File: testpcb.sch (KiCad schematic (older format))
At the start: 14 parts

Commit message: pady poustawiane
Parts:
- added D1, D10, D11, D12, D13, D14, D15, D16, D17, D2, D3, D4, D5, D6, D7, D8, D9: D_Small, Diode_SMD:D_SOD-123, symbol Device:D_Small
- added F1: 500mA, Fuse:Fuse_1206_3216Metric, symbol Device:Polyfuse_Small
- added MX1, MX10, MX11, MX12, MX13, MX14, MX15, MX2, MX3, MX4, MX6, MX7, MX8, MX9: MX-NoLED, MX_Only:MXOnly-1U, symbol MX_Alps_Hybrid:MX-NoLED
- added MX16, MX17, MX5: MX-NoLED, MX_Only:MXOnly-2U, symbol MX_Alps_Hybrid:MX-NoLED
- added R5, R6: 5k1, Resistor_SMD:R_0815_2038Metric, symbol Device:R_Small
- added USB1: HRO-TYPE-C-31-M-12, Type-C:HRO-TYPE-C-31-M-12-Assembly, symbol Type-C:HRO-TYPE-C-31-M-12
- C1, C2, C3, C4, C5, C6: renamed from C?; footprint (none) -> Capacitor_SMD:C_0805_2012Metric
- C7: renamed from C?; value C_Small -> 1uF; footprint (none) -> Capacitor_SMD:C_0805_2012Metric
- R1, R2, R3, R4: renamed from R?; footprint (none) -> Resistor_SMD:R_0815_2038Metric
- SW1: renamed from SW?; footprint (none) -> random-keyboard-parts:SKQG-1155865
- Y1: renamed from Y?; footprint (none) -> Crystal:Crystal_SMD_3225-4Pin_3.2x2.5mm
- gave numbers to parts that had none: 1
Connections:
- net +5V: now also F1.1
- net D+: now also USB1.6 (DP1), USB1.8 (DP2)
- net D-: now also USB1.5 (DN2), USB1.7 (DN1)
- net GND: now also R5.1, R6.1, USB1.1 (GND)
- new net: R6.2, USB1.10 (CC2)
- new net: R5.2, USB1.4 (CC1)
- new net: D1.2 (A), MX1.2 (ROW)
- new net: D6.2 (A), MX6.2 (ROW)
- new net: D10.2 (A), MX10.2 (ROW)
- new net: D15.2 (A), MX15.2 (ROW)
- new net: D2.2 (A), MX2.2 (ROW)
- new net: D7.2 (A), MX7.2 (ROW)
- new net: D11.2 (A), MX11.2 (ROW)
- new net: D3.2 (A), MX3.2 (ROW)
- new net: D8.2 (A), MX8.2 (ROW)
- new net: D12.2 (A), MX12.2 (ROW)
- new net: D16.2 (A), MX16.2 (ROW)
- new net: D4.2 (A), MX4.2 (ROW)
- new net: D9.2 (A), MX9.2 (ROW)
- new net: D13.2 (A), MX13.2 (ROW)
- new net: D5.2 (A), MX5.2 (ROW)
- new net: D14.2 (A), MX14.2 (ROW)
- new net: D17.2 (A), MX17.2 (ROW)
- new net COL0: MX1.1 (COL), MX2.1 (COL), MX3.1 (COL), MX4.1 (COL), MX5.1 (COL)
- new net COL1: MX6.1 (COL), MX7.1 (COL), MX8.1 (COL), MX9.1 (COL)
- new net COL2: MX10.1 (COL), MX11.1 (COL), MX12.1 (COL), MX13.1 (COL), MX14.1 (COL)
- new net COL3: MX15.1 (COL), MX16.1 (COL), MX17.1 (COL)
- new net ROW0: D1.1 (K), D10.1 (K), D15.1 (K), D6.1 (K)
- new net ROW1: D11.1 (K), D16.1 (K), D2.1 (K), D7.1 (K)
- new net ROW2: D12.1 (K), D3.1 (K), D8.1 (K)
- new net ROW3: D13.1 (K), D17.1 (K), D4.1 (K), D9.1 (K)
- new net ROW4: D14.1 (K), D5.1 (K)
- new net VCC: F1.2, USB1.2 (VBUS)
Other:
- moved on the sheet: C1, C2, C5, C6

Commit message: ulozenie git
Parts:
- R1, R2, R3, R4, R5, R6: footprint Resistor_SMD:R_0815_2038Metric -> Resistor_SMD:R_0805_2012Metric
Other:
- moved on the sheet: C1, C2, C5, C6
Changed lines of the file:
@@
 F 0 "R4" V 4154 5750 50  0000 C CNN
 F 1 "10k" V 4245 5750 50  0000 C CNN
-F 2 "Resistor_SMD:R_0815_2038Metric" H 4350 5750 50  0001 C CNN
+F 2 "Resistor_SMD:R_0805_2012Metric" H 4350 5750 50  0001 C CNN
 F 3 "~" H 4350 5750 50  0001 C CNN
 	1    4350 5750
@@
 F 0 "R2" V 1704 4650 50  0000 C CNN
 F 1 "22" V 1795 4650 50  0000 C CNN
-F 2 "Resistor_SMD:R_0815_2038Metric" H 1900 4650 50  0001 C CNN
+F 2 "Resistor_SMD:R_0805_2012Metric" H 1900 4650 50  0001 C CNN
 F 3 "~" H 1900 4650 50  0001 C CNN
 	1    1900 4650
@@
 F 0 "R1" V 1354 4750 50  0000 C CNN
 F 1 "22" V 1445 4750 50  0000 C CNN
-F 2 "Resistor_SMD:R_0815_2038Metric" H 1550 4750 50  0001 C CNN
+F 2 "Resistor_SMD:R_0805_2012Metric" H 1550 4750 50  0001 C CNN
 F 3 "~" H 1550 4750 50  0001 C CNN
 	1    1550 4750
@@
 L power:+5V #PWR0105
 U 1 1 60AE12C3
-P 1700 1300
-F 0 "#PWR0105" H 1700 1150 50  0001 C CNN
-F 1 "+5V" H 1715 1473 50  0000 C CNN
-F 2 "" H 1700 1300 50  0001 C CNN
-F 3 "" H 1700 1300 50  0001 C CNN
-	1    1700 1300
+P 1950 1350
+F 0 "#PWR0105" H 1950 1200 50  0001 C CNN
+F 1 "+5V" H 1965 1523 50  0000 C CNN
+F 2 "" H 1950 1350 50  0001 C CNN
+F 3 "" H 1950 1350 50  0001 C CNN
+	1    1950 1350
 	1    0    0    -1
 $EndComp
@@
 L Device:C_Small C1
 U 1 1 60AE244A
-P 1100 1500
-F 0 "C1" H 1192 1546 50  0000 L CNN
-F 1 "0.1uF" H 1192 1455 50  0000 L CNN
-F 2 "Capacitor_SMD:C_0805_2012Metric" H 1100 1500 50  0001 C CNN
-F 3 "~" H 1100 1500 50  0001 C CNN
-	1    1100 1500
+P 1350 1550
+F 0 "C1" H 1442 1596 50  0000 L CNN
+F 1 "0.1uF" H 1442 1505 50  0000 L CNN
+F 2 "Capacitor_SMD:C_0805_2012Metric" H 1350 1550 50  0001 C CNN
+F 3 "~" H 1350 1550 50  0001 C CNN
+	1    1350 1550
 	1    0    0    -1
 $EndComp
@@
 L power:GND #PWR0106
 U 1 1 60AE1A76
-P 1700 1700
-F 0 "#PWR0106" H 1700 1450 50  0001 C CNN
-F 1 "GND" H 1705 1527 50  0000 C CNN
-F 2 "" H 1700 1700 50  0001 C CNN
-F 3 "" H 1700 1700 50  0001 C CNN
-	1    1700 1700
+P 1950 1750
+F 0 "#PWR0106" H 1950 1500 50  0001 C CNN
+F 1 "GND" H 1955 1577 50  0000 C CNN
+F 2 "" H 1950 1750 50  0001 C CNN
+F 3 "" H 1950 1750 50  0001 C CNN
+	1    1950 1750
 	1    0    0    -1
 $EndComp
@@
 L Device:C_Small C2
 U 1 1 60AE4BA8
-P 1500 1500
-F 0 "C2" H 1592 1546 50  0000 L CNN
-F 1 "0.1uF" H 1592 1455 50  0000 L CNN
-F 2 "Capacitor_SMD:C_0805_2012Metric" H 1500 1500 50  0001 C CNN
-F 3 "~" H 1500 1500 50  0001 C CNN
-	1    1500 1500
+P 1750 1550
+F 0 "C2" H 1842 1596 50  0000 L CNN
+F 1 "0.1uF" H 1842 1505 50  0000 L CNN
+F 2 "Capacitor_SMD:C_0805_2012Metric" H 1750 1550 50  0001 C CNN
+F 3 "~" H 1750 1550 50  0001 C CNN
+	1    1750 1550
 	1    0    0    -1
 $EndComp
@@
 L Device:C_Small C5
 U 1 1 60AE54EF
-P 1900 1500
-F 0 "C5" H 1992 1546 50  0000 L CNN
-F 1 "0.1uF" H 1992 1455 50  0000 L CNN
-F 2 "Capacitor_SMD:C_0805_2012Metric" H 1900 1500 50  0001 C CNN
-F 3 "~" H 1900 1500 50  0001 C CNN
-	1    1900 1500
+P 2150 1550
+F 0 "C5" H 2242 1596 50  0000 L CNN
+F 1 "0.1uF" H 2242 1505 50  0000 L CNN
+F 2 "Capacitor_SMD:C_0805_2012Metric" H 2150 1550 50  0001 C CNN
+F 3 "~" H 2150 1550 50  0001 C CNN
+	1    2150 1550
 	1    0    0    -1
 $EndComp
@@
 L Device:C_Small C6
 U 1 1 60AE5F61
-P 2300 1500
-F 0 "C6" H 2392 1546 50  0000 L CNN
-F 1 "10uF" H 2392 1455 50  0000 L CNN
-F 2 "Capacitor_SMD:C_0805_2012Metric" H 2300 1500 50  0001 C CNN
-F 3 "~" H 2300 1500 50  0001 C CNN
-	1    2300 1500
-	1    0    0    -1
-$EndComp
-Wire Wire Line
-	1100 1400 1500 1400
-Connection ~ 1500 1400
-Wire Wire Line
-	1500 1400 1700 1400
-Connection ~ 1900 1400
-Wire Wire Line
-	1900 1400 2300 1400
-Wire Wire Line
-	2300 1600 1900 1600
-Connection ~ 1500 1600
-Wire Wire Line
-	1500 1600 1100 1600
-Connection ~ 1900 1600
-Wire Wire Line
-	1900 1600 1700 1600
-Wire Wire Line
-	1700 1700 1700 1600
-Connection ~ 1700 1600
-Wire Wire Line
-	1700 1600 1500 1600
-Wire Wire Line
-	1700 1300 1700 1400
-Connection ~ 1700 1400
-Wire Wire Line
-	1700 1400 1900 1400
+P 2550 1550
+F 0 "C6" H 2642 1596 50  0000 L CNN
+F 1 "10uF" H 2642 1505 50  0000 L CNN
+F 2 "Capacitor_SMD:C_0805_2012Metric" H 2550 1550 50  0001 C CNN
+F 3 "~" H 2550 1550 50  0001 C CNN
+	1    2550 1550
+	1    0    0    -1
+$EndComp
+Wire Wire Line
+	1350 1450 1750 1450
+Connection ~ 1750 1450
+Wire Wire Line
+	1750 1450 1950 1450
+Connection ~ 2150 1450
+Wire Wire Line
+	2150 1450 2550 1450
+Wire Wire Line
+	2550 1650 2150 1650
+Connection ~ 1750 1650
+Wire Wire Line
+	1750 1650 1350 1650
+Connection ~ 2150 1650
+Wire Wire Line
+	2150 1650 1950 1650
+Wire Wire Line
+	1950 1750 1950 1650
+Connection ~ 1950 1650
+Wire Wire Line
+	1950 1650 1750 1650
+Wire Wire Line
+	1950 1350 1950 1450
+Connection ~ 1950 1450
+Wire Wire Line
+	1950 1450 2150 1450
 $Comp
 L power:+5V #PWR0107
@@
 F 0 "R3" H 2759 3196 50  0000 L CNN
 F 1 "10k" H 2759 3105 50  0000 L CNN
-F 2 "Resistor_SMD:R_0815_2038Metric" H 2700 3150 50  0001 C CNN
+F 2 "Resistor_SMD:R_0805_2012Metric" H 2700 3150 50  0001 C CNN
 F 3 "~" H 2700 3150 50  0001 C CNN
 	1    2700 3150
@@
 F 0 "R5" V 6354 3000 50  0000 C CNN
 F 1 "5k1" V 6445 3000 50  0000 C CNN
-F 2 "Resistor_SMD:R_0815_2038Metric" H 6550 3000 50  0001 C CNN
+F 2 "Resistor_SMD:R_0805_2012Metric" H 6550 3000 50  0001 C CNN
 F 3 "~" H 6550 3000 50  0001 C CNN
 	1    6550 3000
@@
 F 0 "R6" V 6354 3300 50  0000 C CNN
 F 1 "5k1" V 6445 3300 50  0000 C CNN
-F 2 "Resistor_SMD:R_0815_2038Metric" H 6550 3300 50  0001 C CNN
+F 2 "Resistor_SMD:R_0805_2012Metric" H 6550 3300 50  0001 C CNN
 F 3 "~" H 6550 3300 50  0001 C CNN
 	1    6550 3300

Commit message: jakies poprawki chyba
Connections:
- net GND: now also USB1.12 (GND), USB1.13 (SHIELD)
- net VCC: now also USB1.11 (VBUS)
- no-connect marks 0 -> 2
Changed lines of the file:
@@
 Text GLabel 6250 2900 2    50   Input ~ 0
 D+
+NoConn ~ 5850 2600
+NoConn ~ 5850 3200
+$Comp
+L power:GND #PWR0115
+U 1 1 60B55626
+P 6100 3500
+F 0 "#PWR0115" H 6100 3250 50  0001 C CNN
+F 1 "GND" H 6105 3327 50  0000 C CNN
+F 2 "" H 6100 3500 50  0001 C CNN
+F 3 "" H 6100 3500 50  0001 C CNN
+	1    6100 3500
+	1    0    0    -1
+$EndComp
+Wire Wire Line
+	5850 3500 6100 3500
+Wire Wire Line
+	5850 3600 5850 3500
+Connection ~ 5850 3500
+$Comp
+L power:VCC #PWR0116
+U 1 1 60B6523D
+P 6300 3450
+F 0 "#PWR0116" H 6300 3300 50  0001 C CNN
+F 1 "VCC" H 6315 3623 50  0000 C CNN
+F 2 "" H 6300 3450 50  0001 C CNN
+F 3 "" H 6300 3450 50  0001 C CNN
+	1    6300 3450
+	1    0    0    -1
+$EndComp
+Wire Wire Line
+	5850 3400 6250 3400
+Wire Wire Line
+	6250 3400 6250 3450
+Wire Wire Line
+	6250 3450 6300 3450
 $EndSCHEMATC

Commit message: polaczone switche / wizualne poprawki tracerow
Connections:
- net COL0: now also U1.28 (PB4)
- net COL1: now also U1.27 (PD7)
- net COL2: now also U1.26 (PD6)
- net COL3: now also U1.25 (PD4)
- net ROW0: now also U1.36 (PF7)
- net ROW1: now also U1.37 (PF6)
- net ROW2: now also U1.38 (PF5)
- net ROW3: now also U1.39 (PF4)
- net ROW4: now also U1.40 (PF1)
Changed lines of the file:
@@
 Wire Wire Line
 	6250 3450 6300 3450
+Wire Wire Line
+	3900 5550 4100 5550
+Wire Wire Line
+	3900 5450 4100 5450
+Wire Wire Line
+	3900 5250 4100 5250
+Wire Wire Line
+	3900 4050 4150 4050
+Text GLabel 4100 5250 2    50   Input ~ 0
+COL3
+Text GLabel 4100 5450 2    50   Input ~ 0
+COL2
+Text GLabel 4100 5550 2    50   Input ~ 0
+COL1
+Text GLabel 4150 4050 2    50   Input ~ 0
+COL0
+Wire Wire Line
+	3900 6550 4200 6550
+Wire Wire Line
+	3900 6450 4200 6450
+Wire Wire Line
+	3900 6350 4200 6350
+Wire Wire Line
+	3900 6250 4200 6250
+Wire Wire Line
+	3900 6150 4200 6150
+Text GLabel 4200 6550 2    50   Input ~ 0
+ROW0
+Text GLabel 4200 6450 2    50   Input ~ 0
+ROW1
+Text GLabel 4200 6350 2    50   Input ~ 0
+ROW2
+Text GLabel 4200 6250 2    50   Input ~ 0
+ROW3
+Text GLabel 4200 6150 2    50   Input ~ 0
+ROW4
 $EndSCHEMATC

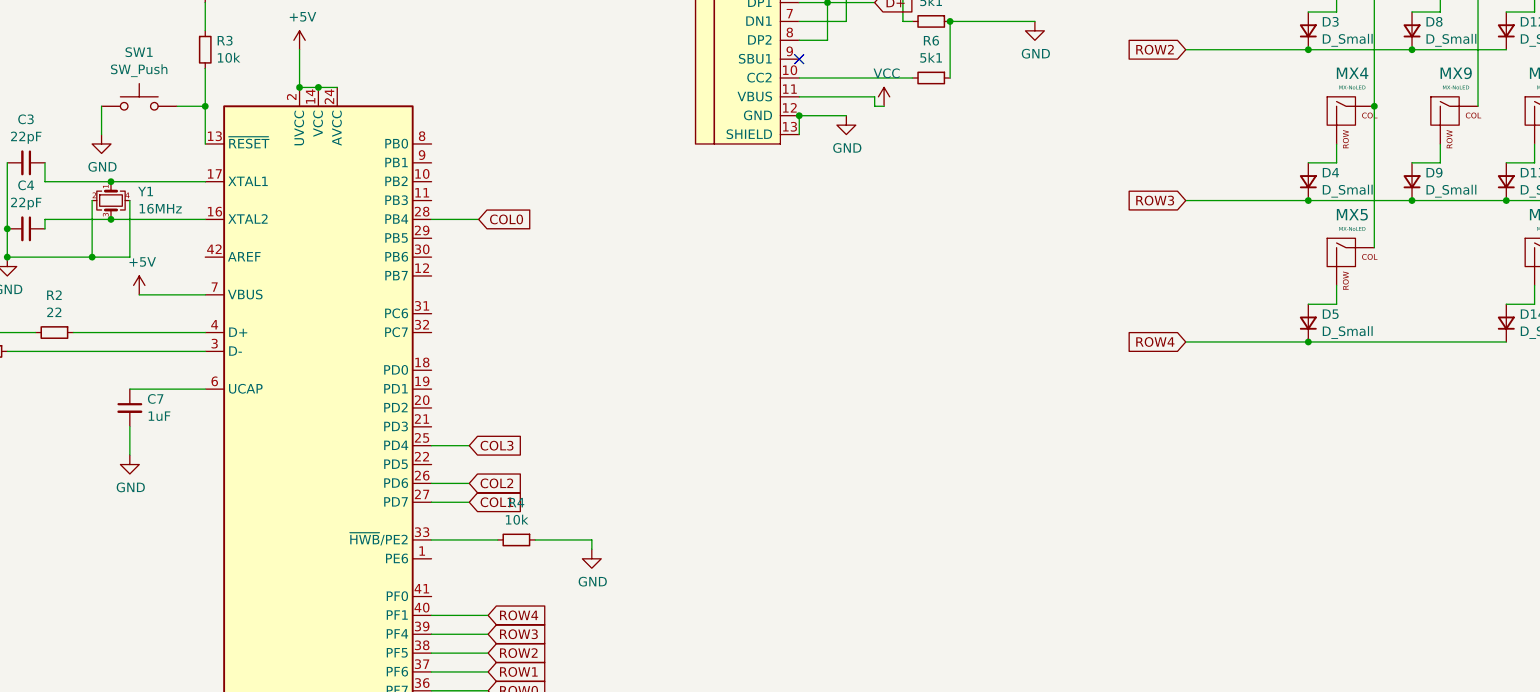
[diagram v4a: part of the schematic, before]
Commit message: mounting holes
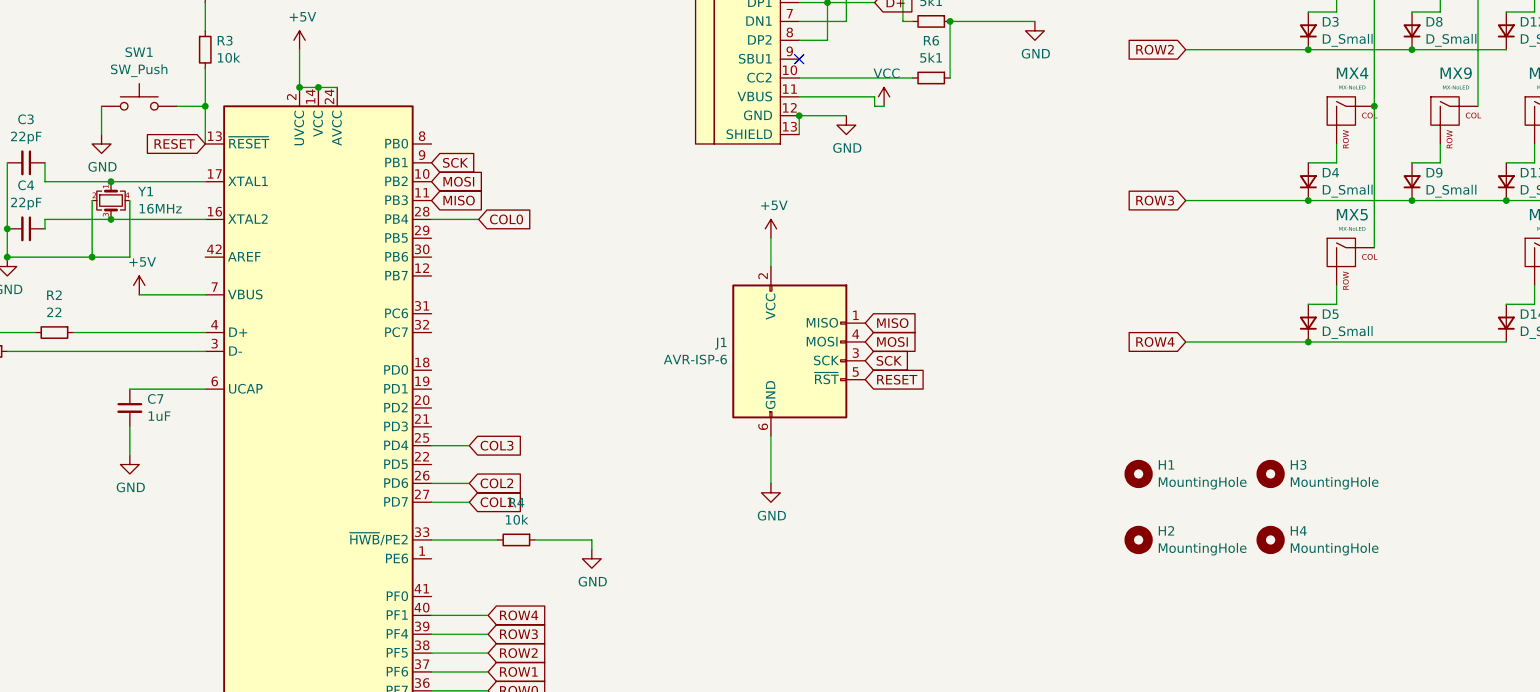
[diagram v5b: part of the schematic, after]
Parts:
- added H1, H2, H3, H4: MountingHole, MountingHole:MountingHole_2.1mm, symbol Mechanical:MountingHole
- added J1: AVR-ISP-6, random-keyboard-parts:Reset_Pretty-Mask, symbol Connector:AVR-ISP-6
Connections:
- net +5V: now also J1.2 (VCC)
- net GND: now also J1.6 (GND)
- net MOSI: now reaches U1.10 (PB2)
- net MOSI: now also J1.4 (MOSI)
- net MISO: now reaches U1.11 (PB3)
- net MISO: now also J1.1 (MISO)
- net RESET: now reaches R3.2, SW1.2, U1.13 (~RESET)
- net RESET: now also J1.5 (~RST)
- net SCK: now reaches U1.9 (PB1)
- net SCK: now also J1.3 (SCK)
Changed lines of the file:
@@
 Text GLabel 4200 6150 2    50   Input ~ 0
 ROW4
+$Comp
+L Connector:AVR-ISP-6 J1
+U 1 1 60B2F9FE
+P 5800 4800
+F 0 "J1" H 5471 4896 50  0000 R CNN
+F 1 "AVR-ISP-6" H 5471 4805 50  0000 R CNN
+F 2 "random-keyboard-parts:Reset_Pretty-Mask" V 5550 4850 50  0001 C CNN
+F 3 " ~" H 4525 4250 50  0001 C CNN
+	1    5800 4800
+	1    0    0    -1
+$EndComp
+Wire Wire Line
+	5700 4300 5700 4150
+Wire Wire Line
+	5700 5200 5700 5450
+$Comp
+L power:GND #PWR0117
+U 1 1 60B3C1DE
+P 5700 5450
+F 0 "#PWR0117" H 5700 5200 50  0001 C CNN
+F 1 "GND" H 5705 5277 50  0000 C CNN
+F 2 "" H 5700 5450 50  0001 C CNN
+F 3 "" H 5700 5450 50  0001 C CNN
+	1    5700 5450
+	1    0    0    -1
+$EndComp
+$Comp
+L power:+5V #PWR0118
+U 1 1 60B3D4A1
+P 5700 4150
+F 0 "#PWR0118" H 5700 4000 50  0001 C CNN
+F 1 "+5V" H 5715 4323 50  0000 C CNN
+F 2 "" H 5700 4150 50  0001 C CNN
+F 3 "" H 5700 4150 50  0001 C CNN
+	1    5700 4150
+	1    0    0    -1
+$EndComp
+Text GLabel 2700 3650 0    50   Input ~ 0
+RESET
+Text GLabel 6200 4900 2    50   Input ~ 0
+RESET
+Text GLabel 6200 4600 2    50   Input ~ 0
+MISO
+Text GLabel 6200 4700 2    50   Input ~ 0
+MOSI
+Text GLabel 6200 4800 2    50   Input ~ 0
+SCK
+Text GLabel 3900 3950 2    50   Input ~ 0
+MISO
+Text GLabel 3900 3850 2    50   Input ~ 0
+MOSI
+Text GLabel 3900 3750 2    50   Input ~ 0
+SCK
+$Comp
+L Mechanical:MountingHole H1
+U 1 1 60B94DE7
+P 7650 5400
+F 0 "H1" H 7750 5446 50  0000 L CNN
+F 1 "MountingHole" H 7750 5355 50  0000 L CNN
+F 2 "MountingHole:MountingHole_2.1mm" H 7650 5400 50  0001 C CNN
+F 3 "~" H 7650 5400 50  0001 C CNN
+	1    7650 5400
+	1    0    0    -1
+$EndComp
+$Comp
+L Mechanical:MountingHole H3
+U 1 1 60B9588C
+P 8350 5400
+F 0 "H3" H 8450 5446 50  0000 L CNN
+F 1 "MountingHole" H 8450 5355 50  0000 L CNN
+F 2 "MountingHole:MountingHole_2.1mm" H 8350 5400 50  0001 C CNN
+F 3 "~" H 8350 5400 50  0001 C CNN
+	1    8350 5400
+	1    0    0    -1
+$EndComp
+$Comp
+L Mechanical:MountingHole H2
+U 1 1 60B95EE4
+P 7650 5750
+F 0 "H2" H 7750 5796 50  0000 L CNN
+F 1 "MountingHole" H 7750 5705 50  0000 L CNN
+F 2 "MountingHole:MountingHole_2.1mm" H 7650 5750 50  0001 C CNN
+F 3 "~" H 7650 5750 50  0001 C CNN
+	1    7650 5750
+	1    0    0    -1
+$EndComp
+$Comp
+L Mechanical:MountingHole H4
+U 1 1 60B9617C
+P 8350 5750
+F 0 "H4" H 8450 5796 50  0000 L CNN
+F 1 "MountingHole" H 8450 5705 50  0000 L CNN
+F 2 "MountingHole:MountingHole_2.1mm" H 8350 5750 50  0001 C CNN
+F 3 "~" H 8350 5750 50  0001 C CNN
+	1    8350 5750
+	1    0    0    -1
+$EndComp
 $EndSCHEMATC
